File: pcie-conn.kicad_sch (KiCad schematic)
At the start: 22 parts, among them J2 1-2199230-6

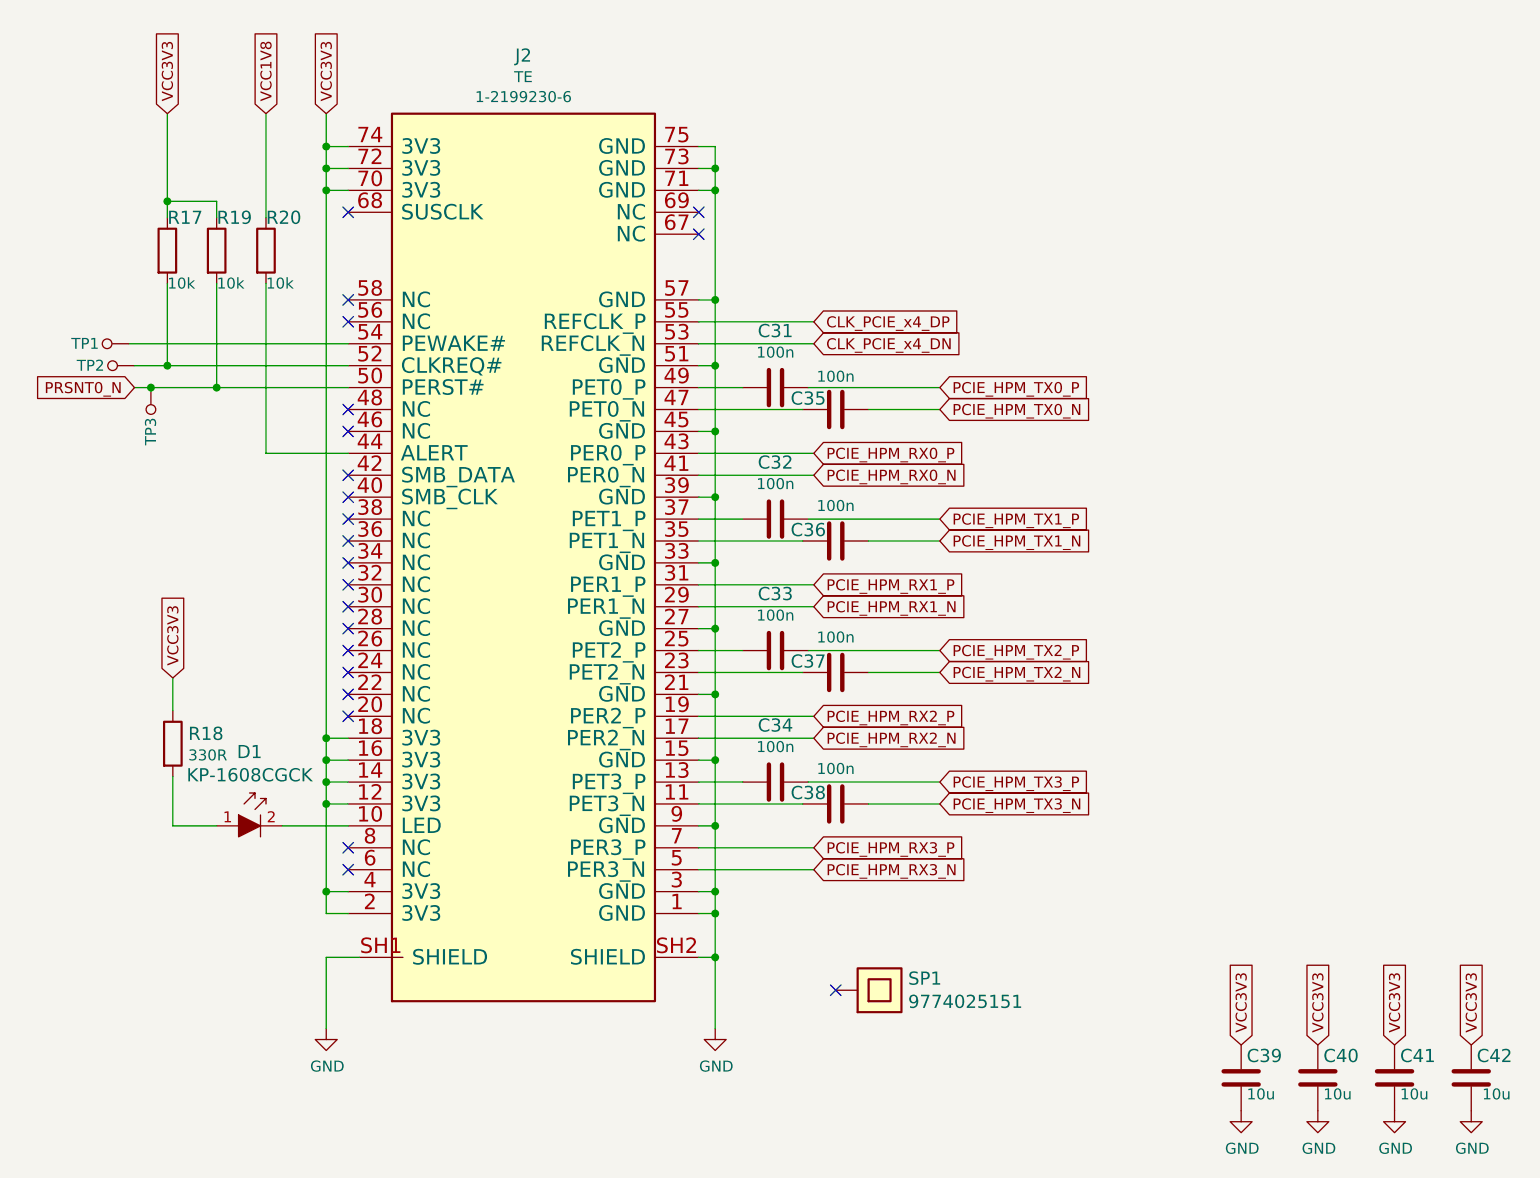
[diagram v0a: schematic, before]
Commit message: [#61392] Convert project to KiCad 7
[#61392] Run globlib

[#61392] Allign components to the grid

[#61392] Update oshw and antmicro logo

[#61392] Standarize ethernet sheet

[#61392] Standarize pcie-conn sheet

[#61392] Standarize rot sheet

[#61392] Standarize edge-connector sheet

[#61392] WIP:Standarize interfaces sheet

[#61392] WIP: Route interfaces sheet

[#61392] Finish standarizing interfaces sheet

[#61392] Update interfaces sheet with fixed 2N7002

[#61392] WIP:Standarize ddr3 sheet

[#61392] Standarize ddr3 sheet

[#61392] Standarize power-supply sheet

[#61392] Standarize fpga power-supply sheet

[#61392] Remove TODO comments from power-banks sheet

[#61392] Standarize fpga-banks sheet

[#61392] Ignore Input pins not driven ERC

[#61392] Clear off grid ERCs

[#61392] Exclude ERC DDR3_VTT_EN NC

[#61392] Bump rev to 1.2.1

[#61392] Bump PCB rev to 1.2.1
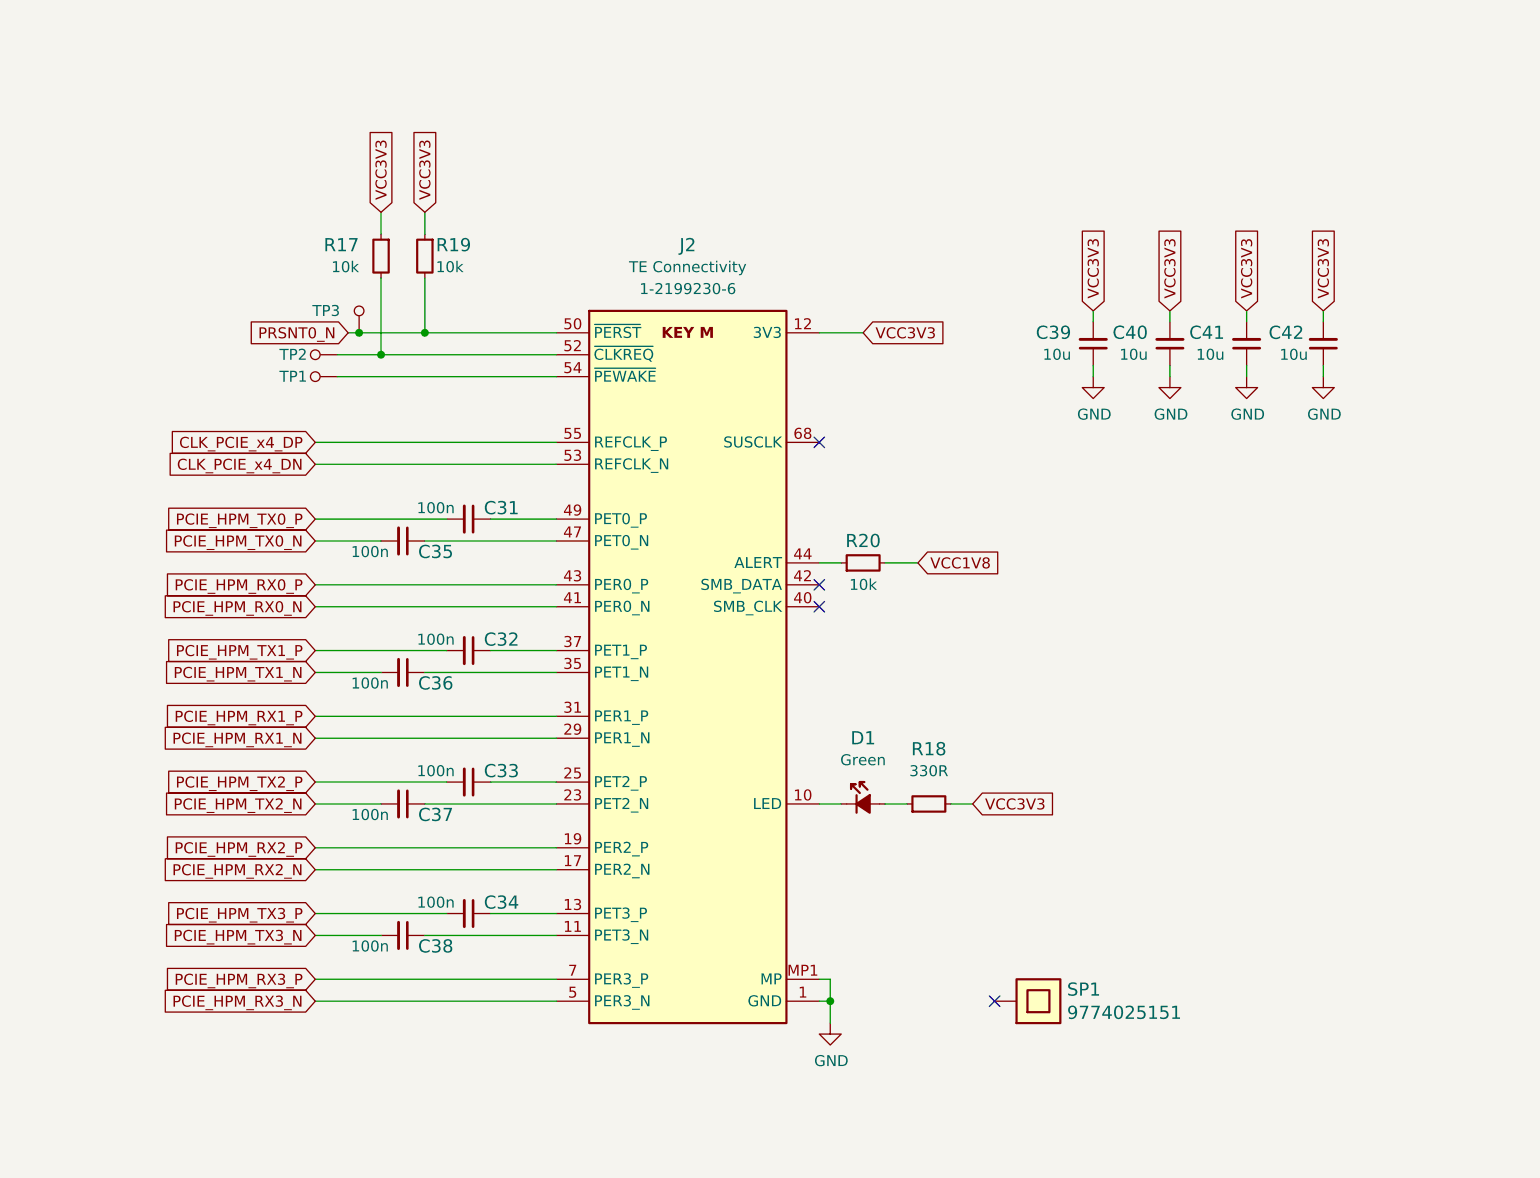
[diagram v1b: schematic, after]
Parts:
- C31, C32, C33, C34, C35, C36, C37, C38: footprint ecp5-dc-scm-footprints:0402-cap -> antmicro-footprints:C_0402_1005Metric; symbol ecp5-dc-scm:C_100n_0402 -> antmicroCapacitors0402:C_100n_0402; Author (none) -> Antmicro; Dielectric (none) -> X5R; License (none) -> Apache-2.0; MPN 0402X104K6R3CT -> GRM155R61H104KE14D; Manufacturer Walsin -> Murata; Public (none) -> False; Voltage (none) -> 50V
- C39, C40, C41, C42: footprint ecp5-dc-scm-footprints:0402-cap -> antmicro-footprints:C_0402_1005Metric; symbol ecp5-dc-scm:C_10u_0402 -> antmicroCapacitors0402:C_10u_0402; Author (none) -> Antmicro; License (none) -> Apache-2.0; MPN GRM155R60J106ME44D -> CC0402MRX5R5BB106; Manufacturer MURATA -> YAGEO; Public (none) -> False
- D1: value KP-1608CGCK -> LED_G_0603_KP-1608CGCK; footprint ecp5-dc-scm-footprints:LED_0603 -> antmicro-footprints:LED_0603_1608Metric_G; symbol ecp5-dc-scm:KP-1608CGCK -> antmicroLEDIndicationDiscrete:LED_G_0603_KP-1608CGCK; Author (none) -> Antmicro; Color (none) -> Green; License (none) -> Apache-2.0; Manufacturer KINGBRIGHT -> Kingbright; Public (none) -> False
- J2: value 1-2199230-6 -> Bus_M.2_1-2199230-6; footprint ecp5-dc-scm-footprints:1-2199230-6 -> antmicro-footprints:Bus_M.2_Socket_Key_M_TE_1-2199230-6; symbol ecp5-dc-scm:1-2199230-6 -> antmicroPciConnectors:Bus_M.2_1-2199230-6; Author (none) -> Antmicro; License (none) -> Apache-2.0; Manufacturer TE -> TE Connectivity
- R17, R19, R20: footprint ecp5-dc-scm-footprints:0402-res -> antmicro-footprints:R_0402_1005Metric; symbol ecp5-dc-scm:R_10k_0402 -> antmicroResistors0402:R_10k_0402; Author (none) -> Antmicro; License (none) -> Apache-2.0; MPN CRCW040210K0FKEDHP -> CR0402-FX-1002GLF; Manufacturer VISHAY -> Bourns; Public (none) -> False; Tolerance (none) -> 1%
- R18: footprint ecp5-dc-scm-footprints:0402-res -> antmicro-footprints:R_0402_1005Metric; symbol ecp5-dc-scm:R_330R_0402 -> antmicroResistors0402:R_330R_0402; Author (none) -> Antmicro; License (none) -> Apache-2.0; MPN MCMR04X3300FTL -> CR0402-FX-3300GLF; Manufacturer MULTICOMP -> Bourns; Public (none) -> False; Tolerance (none) -> 1%
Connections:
- net GND: now also C39.1, C40.1, C41.1, C42.1, J2.MP1 (MP), J2.MP2 (MP); no longer C39.2, C40.2, C41.2, C42.2, J2.SH1 (SHIELD), J2.SH2 (SHIELD)
- net VCC1V8: now also R20.2; no longer R20.1
- net VCC3V3: now also C39.2, C40.2, C41.2, C42.2, R18.2; no longer C39.1, C40.1, C41.1, C42.1, R18.1
- net at J2.10 (LED): now also D1.1 (C); no longer D1.2
- net at J2.44 (ALERT): now also R20.1; no longer R20.2
- new net: D1.2 (A), R18.1
- no-connect marks 22 -> 4
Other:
- moved on the sheet: C31, C32, C33, C34, C35, C36, C37, C38, C39, C40, C41, C42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

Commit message: [#61392] Import changes to the PCB
[#61392] Fix D2 orientation

[#61392] Fix J2 J1 D6 orientation

[#61392] WIP: PCB Fix caps orienations

[#61392] PCB Fix caps orienations

[#61392] Fix missalligned edge cuts

[#61392] Sync Sch with PCB

[#61392] Fix silk clipped by edge cuts

[#61392] Ignore TP no courtyard drc

[#61392] Update C_0603 footprints

[#61392] Update R_0402 footprints

[#61392] Update Sot-23 footprints

[#61392] Update QFN and IHLP footprints

[#61392] Update remaining footprints

[#61392] Change minimal text height to 0.7mm

[#61392] Clear remaining Silk DRCs

[#61392] Update TPS51200DRCT symbol

[#61392] Update 9774040151

[#61392] Update W25Q32JVS

[#61392] Update ECS-3225MVQ-1000CN-TR

[#61392] Clean ERC

[#61392] Remove obsolete files

[#61392] Synhronize components with library

[#61392] Remove globlib leftovers

[#61392] Synchronize components with libraries (WiP)

[#61392] Clean ERC and DRC

[#61392] Set J5 to DNP

[#61392] Add PCB SHA string, update layer names

[#61392] Update assets

[#62567] Add stackup.csv

[#62567] Input elecric constants for the board stackup

[#62567] Update stackup.csv
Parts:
- removed D1: LED_G_0603_KP-1608CGCK, antmicro-footprints:LED_0603_1608Metric_G, symbol antmicroLEDIndicationDiscrete:LED_G_0603_KP-1608CGCK
- removed SP1: 9774025151, ecp5-dc-scm-footprints:9774025151, symbol ecp5-dc-scm:9774025151
- removed TP1, TP2, TP3: TP_SMD1MM, ecp5-dc-scm-footprints:Testpoint_smd_1mm, symbol ecp5-dc-scm:TP_SMD1MM
- added D1: LED_G_0603_LG_L29K-G2J1-24-Z, antmicro-footprints:LED_0603_1608Metric_G, symbol antmicroLEDIndicationDiscrete:LED_G_0603_LG_L29K-G2J1-24-Z
- added H1: Spacer_Drill3.7mm_H2.5mm_9774025151R, antmicro-footprints:Spacer_Drill3.7mm_H2.5mm_9774025151R, symbol antmicroMechanicalParts:Spacer_Drill3.7mm_H2.5mm_9774025151R
- added TP1, TP2, TP3: TP_1mm_SMD, antmicro-footprints:TP_SMD_1mm, symbol antmicroTestPoints:TP_1mm_SMD
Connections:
- net PRSNT0_N: now also TP3.1
- net at J2.10 (LED): now also D1.1 (C)
- net at J2.52 (~{CLKREQ}), R17.2: now also TP2.1
- net at J2.54 (~{PEWAKE}): now also TP1.1
- net at R18.1: now also D1.2 (A)
